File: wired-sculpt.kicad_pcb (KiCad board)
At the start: 2 copper layers, 40 x 50 mm, 26 parts, among them J1 10103594-0001LF, J3 AVR-ISP-6 - NOT FITTED, J4 3-84952-0, SW1 FSMSM, U1 AT90USB1286-AU, U2 USBLC6-2SC6, Y1 TSX-3225 16.0000MF18X-AC6

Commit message: WIP: checkpoint work on rev 3 of the schematic and layout
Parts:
- removed R4, R5, R6: ERJ-3GEYJ331V, Resistor_SMD:R_0603_1608Metric
- added C10: CL10A105KA8NNNC, Capacitor_SMD:C_0603_1608Metric, F.Cu at (157.2, 60.6)
- added C11: CL10A105KA8NNNC, Capacitor_SMD:C_0603_1608Metric, F.Cu at (156.2, 53.0)
- added C12: CL10A105KA8NNNC, Capacitor_SMD:C_0603_1608Metric, F.Cu at (157.7, 53.0)
- added C2: CL21B104KACNNNC, Capacitor_SMD:C_0805_2012Metric, F.Cu at (146.8, 67.0)
- added C3: CL21B103KBANNNC, Capacitor_SMD:C_0805_2012Metric, F.Cu at (146.8, 65.0)
- added Q1: BSS84AK,215, Package_TO_SOT_SMD:SOT-23, F.Cu at (137.4, 36.5)
- added Q2: 2N7002, Package_TO_SOT_SMD:SOT-23, F.Cu at (134.8, 40.1)
- added R10: ERJ-PA3J473V, Resistor_SMD:R_0603_1608Metric, F.Cu at (137.5, 34.0)
- added R11: ERJ-3GEYJ331V, Resistor_SMD:R_0603_1608Metric, F.Cu at (151.7, 41.7)
- added R12: ERJ-3EKF10R0V, Resistor_SMD:R_0603_1608Metric, F.Cu at (137.6, 40.1)
- added R13: ERJ-PA3J472V, Resistor_SMD:R_0603_1608Metric, F.Cu at (139.4, 40.1)
- added R7: ERJ-3EKF8873V, Resistor_SMD:R_0603_1608Metric, F.Cu at (145.2, 62.2)
- added SW2: Conn_01x02_Female, Connector_JST:JST_PH_S2B-PH-K_1x02_P2.00mm_Horizontal, F.Cu at (155.5, 67.0)
- added U3: LM2776, Package_TO_SOT_SMD:SOT-23-6, F.Cu at (156.7, 57.3)
- C1: value TAJA106K006RNJ -> CL21A475KAQNNNE; footprint Capacitor_Tantalum_SMD:CP_EIA-3216-10_Kemet-I -> Capacitor_SMD:C_0805_2012Metric
- C5, C6, C7: value CL05A104KA5NNNC -> CL10B104KB8NNNC; footprint Capacitor_SMD:C_0402_1005Metric -> Capacitor_SMD:C_0603_1608Metric
- R2: value ERJ-3EKF2200V -> ERJ-3GEYJ331V
- R8: value ERJ-3EKF1001V -> ERJ-3GEYJ103V
- moved D1 14.9 mm to (153.7, 35.4)
- moved U2 13.6 mm to (151.0, 71.9), turned to 90 degrees
- moved R2 12.3 mm to (151.7, 35.5), turned to 90 degrees
- moved J3 10.4 mm to (134.8, 76.4), turned to 90 degrees
- moved C1 8.35 mm to (146.8, 69.0), turned to 0 degrees
- moved R9 7.36 mm to (157.8, 47.0), turned to 90 degrees
- moved R1 6.04 mm to (151.8, 67.2)
- moved R8 6.00 mm to (133.8, 60.0)
- moved R3 5.95 mm to (150.1, 67.2)
- moved C4 2.35 mm to (154.4, 53.0), turned to 270 degrees
- moved C9 1.68 mm to (147.0, 38.0), turned to 135 degrees
- moved C8 1.65 mm to (142.2, 37.5), turned to 45 degrees
- moved Y1 0.92 mm to (144.6, 39.8), turned to 315 degrees
- moved C7 0.66 mm to (140.8, 62.2)
- moved C6 0.45 mm to (148.2, 41.5), turned to 0 degrees
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- renumbered C2 to C8, C3 to C9
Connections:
- C1 pad 1: VBUS -> GND
- C1 pad 2: GND -> VBUS
- J1 pad 2: Din- -> /Din-
- J1 pad 3: Din+ -> /Din+
- J3 pad 1: Net-(J3-Pad1) -> MISO
- J3 pad 3: Net-(J3-Pad3) -> SCK
- J3 pad 4: Net-(J3-Pad4) -> MOSI
- J4 pad 2: Net-(J4-Pad2) -> RED+
- J4 pad 3: Net-(J4-Pad3) -> GREEN-
- J4 pad MP: GND -> (no net)
- R1 pad 1: Net-(R1-Pad1) -> /D+
- R1 pad 2: Din+ -> /Dout+
- R3 pad 1: Net-(R3-Pad1) -> /D-
- R3 pad 2: Din- -> /Dout-
- R9 pad 1: Net-(R9-Pad1) -> RST
- R9 pad 2: RST -> Net-(R9-Pad2)
- SW1 pad 1: Net-(R9-Pad1) -> GND
- SW1 pad 2: GND -> Net-(R9-Pad2)
- U1 pad 10: Net-(U1-Pad10) -> PB0
- U1 pad 16: Net-(U1-Pad16) -> GREEN+
- U1 pad 17: Net-(U1-Pad17) -> RED+
- U1 pad 26: Net-(J4-Pad2) -> Net-(U1-Pad26)
- U1 pad 27: Net-(J4-Pad3) -> Net-(U1-Pad27)
- U1 pad 4: D- -> /D-
- U1 pad 5: D+ -> /D+
- U2 pad 1: D+ -> /Din-
- U2 pad 3: D- -> /Din+
- U2 pad 4: Net-(R3-Pad1) -> /Dout+
- U2 pad 6: Net-(R1-Pad1) -> /Dout-
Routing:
- net VBUS: track 75.5 -> 183.6 mm
- net Net-(R9-Pad2): track 0.00 -> 27.9 mm
- net RST: track 39.8 -> 12.6 mm
- net Net-(J3-Pad3): track 17.4 -> 0.00 mm
- net Net-(J4-Pad2): track 16.7 -> 0.00 mm
- net MOSI: track 22.1 -> 6.41 mm, vias 2 -> 0
- net Net-(J4-Pad3): track 15.6 -> 0.00 mm
- net /D+: track 0.00 -> 15.6 mm
- net /D-: track 0.00 -> 14.9 mm
- net MISO: track 23.4 -> 8.58 mm, vias 2 -> 0
- net Din-: track 13.4 -> 0.00 mm
- net Din+: track 13.1 -> 0.00 mm
- net PB0: track 0.00 -> 11.4 mm, vias 0 -> 2
- net SCK: track 21.1 -> 9.86 mm, vias 2 -> 0
- net Net-(J3-Pad1): track 9.49 -> 0.00 mm
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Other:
- board text added: "Wired Sculpt 0.3 Chad Austin 2020-03-06"
- board text removed: "Wired Sculpt 0.2 Chad Austin 2020-12-20"

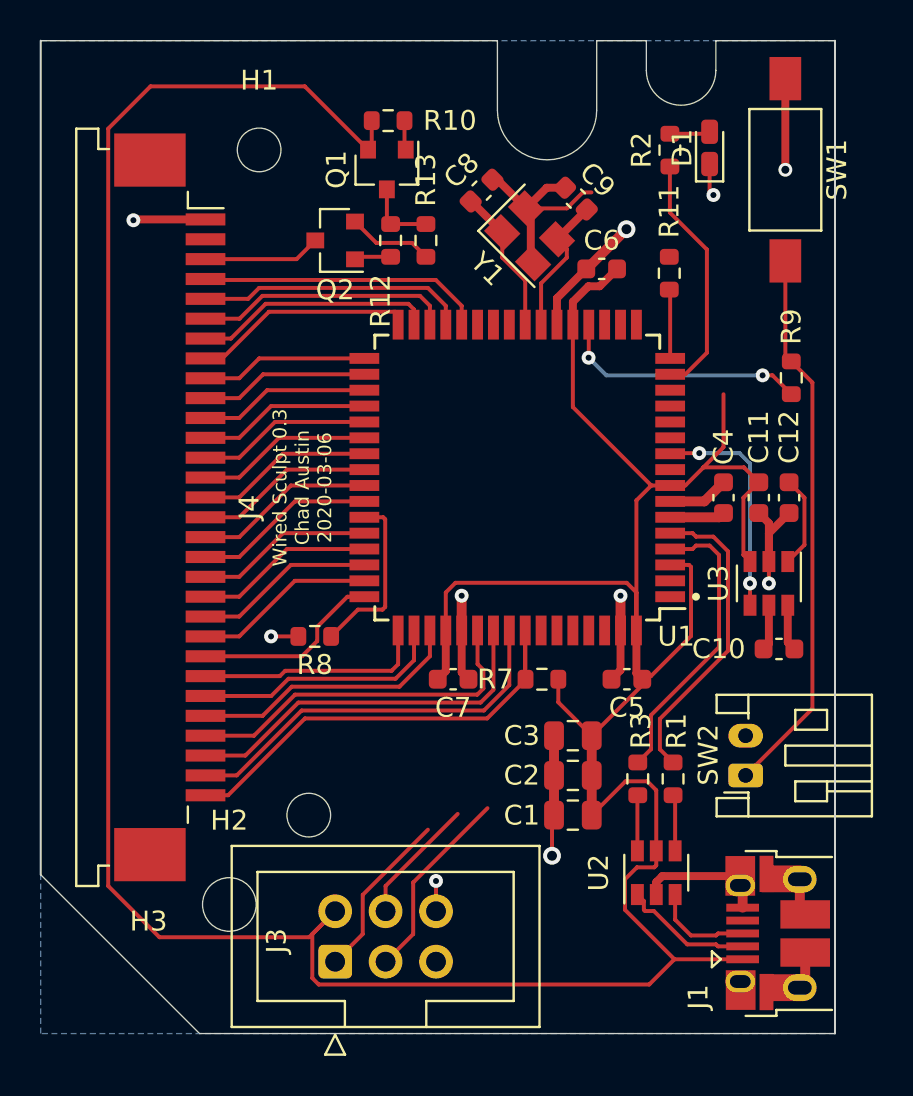
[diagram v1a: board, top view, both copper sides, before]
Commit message: renumber the references
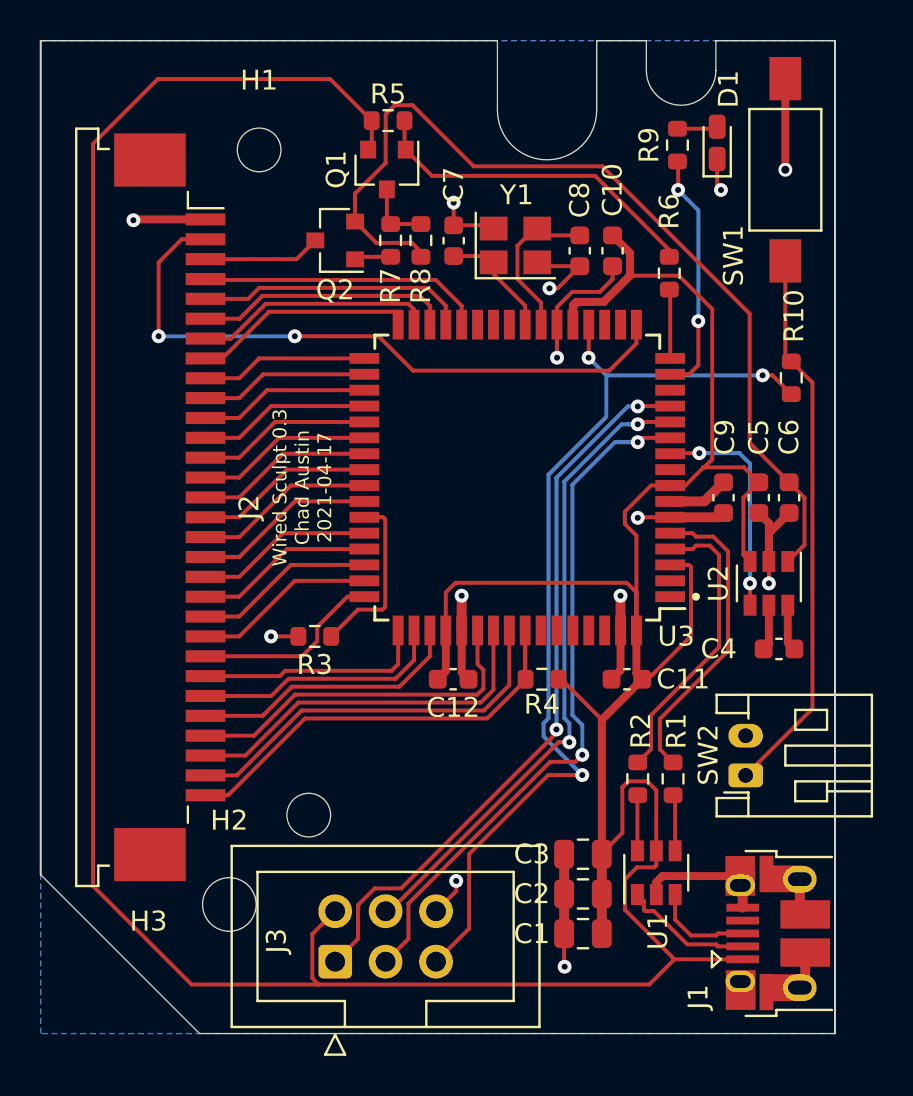
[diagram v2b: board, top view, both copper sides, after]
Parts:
- removed the R2 at (151.7, 35.5)
- added R9: ERJ-3GEYJ331V, Resistor_SMD:R_0603_1608Metric, F.Cu at (152.1, 35.3)
- moved C1 5.99 mm to (147.3, 75.0)
- moved C2 5.99 mm to (147.3, 73.0)
- moved C3 5.99 mm to (147.3, 71.0)
- moved C7 2.89 mm to (140.8, 40.1), turned to 90 degrees
- moved C8 2.63 mm to (147.1, 40.6), turned to 270 degrees
- moved C10 1.06 mm to (148.8, 40.6), turned to 90 degrees
- moved Y1 0.86 mm to (143.9, 40.3), turned to 0 degrees
- moved D1 0.46 mm to (154.1, 35.1)
- moved R8 0.25 mm to (139.1, 40.1)
- renumbered C6 to C10, C5 to C11, C7 to C12, C10 to C4, C11 to C5, C12 to C6, C8 to C7, C9 to C8, C4 to C9, J4 to J2, R9 to R10, R3 to R2, R8 to R3, R7 to R4, R10 to R5, R11 to R6, R12 to R7, R13 to R8, U2 to U1, U3 to U2, U1 to U3
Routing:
- net -5V: track 8.97 -> 47.2 mm
- net RST: track 12.6 -> 48.3 mm, vias 2 -> 3
- net RED+: track 0.00 -> 32.9 mm, vias 0 -> 2
- net MISO: track 8.58 -> 37.0 mm, vias 0 -> 2
- net MOSI: track 6.41 -> 33.1 mm, vias 0 -> 2
- net SCK: track 9.86 -> 35.0 mm, vias 0 -> 2
- net Net-(Q1-Pad1): track 1.49 -> 17.2 mm
- net VBUS: track 183.6 -> 198.2 mm
- net GND: track 64.6 -> 62.8 mm, vias 10 -> 13
- net Net-(C7-Pad1): track 7.36 -> 5.94 mm
- net Net-(C8-Pad1): track 7.16 -> 8.11 mm
- net LED: track 12.5 -> 12.4 mm, vias 0 -> 2
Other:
- board text added: "Wired Sculpt 0.3 Chad Austin 2021-04-17"
- board text removed: "Wired Sculpt 0.3 Chad Austin 2020-03-06"

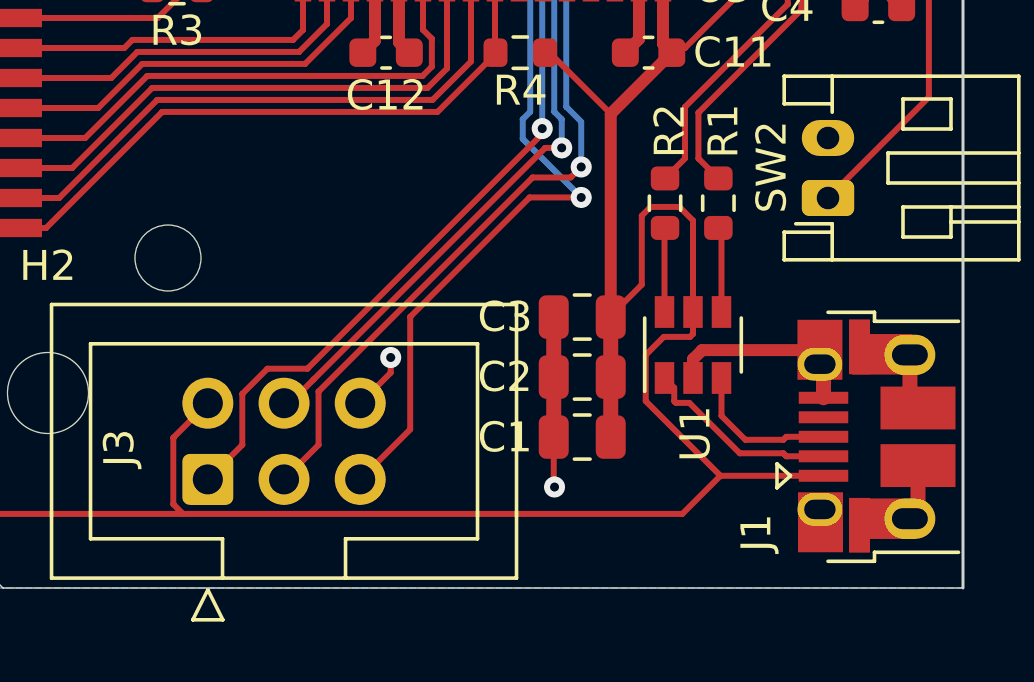
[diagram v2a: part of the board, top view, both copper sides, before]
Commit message: Move a trace and generate gerbers for Apr 18
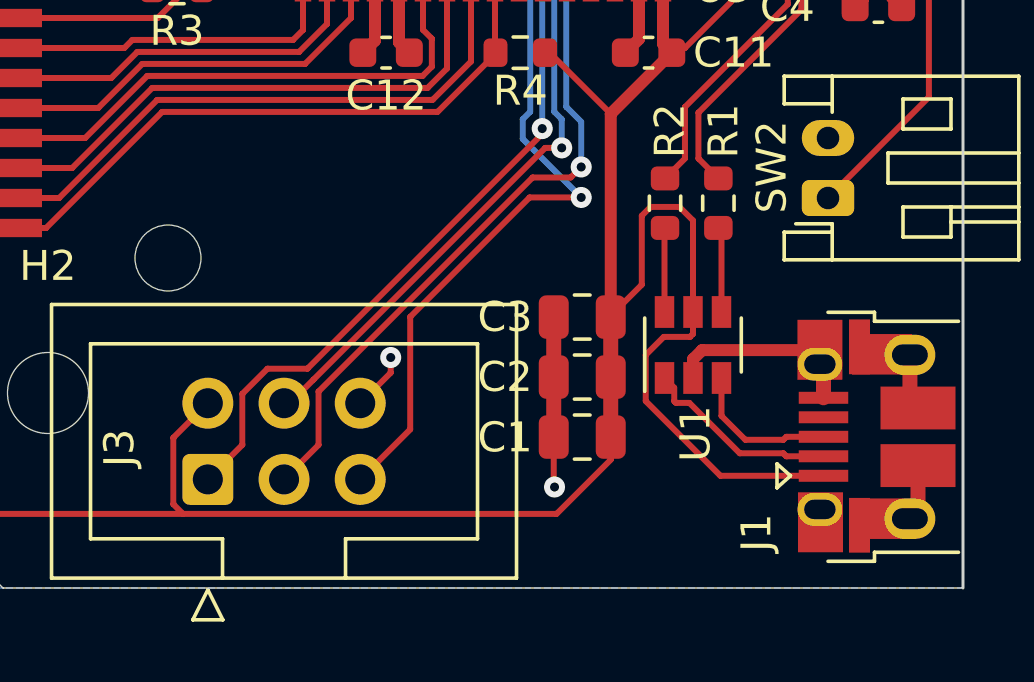
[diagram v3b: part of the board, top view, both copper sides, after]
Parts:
- J2: value 3-84952-0 -> FFC3B07-30-T
- Q2: value 2N7002 -> 2N7002BK
- R3: value ERJ-3GEYJ103V -> ERJ-PA3J472V
- SW2: value Conn_01x02_Female -> S2B-PH-K-S(LF)(SN)
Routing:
- net VBUS: track 198.2 -> 195.5 mm
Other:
- rule pad_to_mask_clearance: 0 -> 0.0508

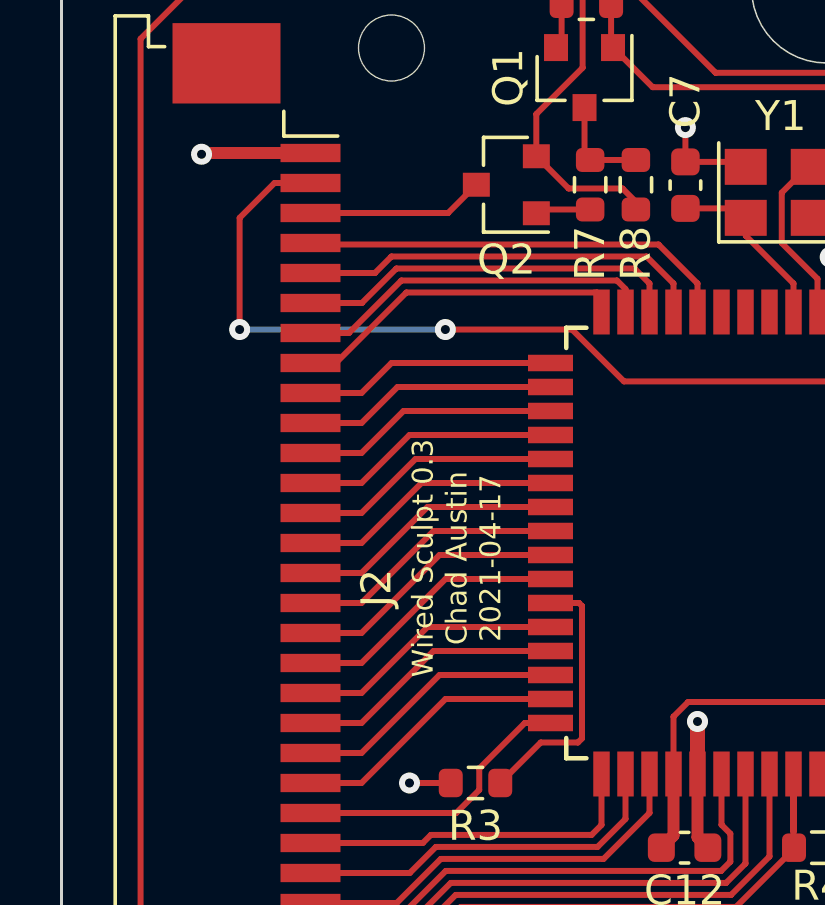
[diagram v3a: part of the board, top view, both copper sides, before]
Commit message: Fix Green- and Red+ pins which were backwards. :(
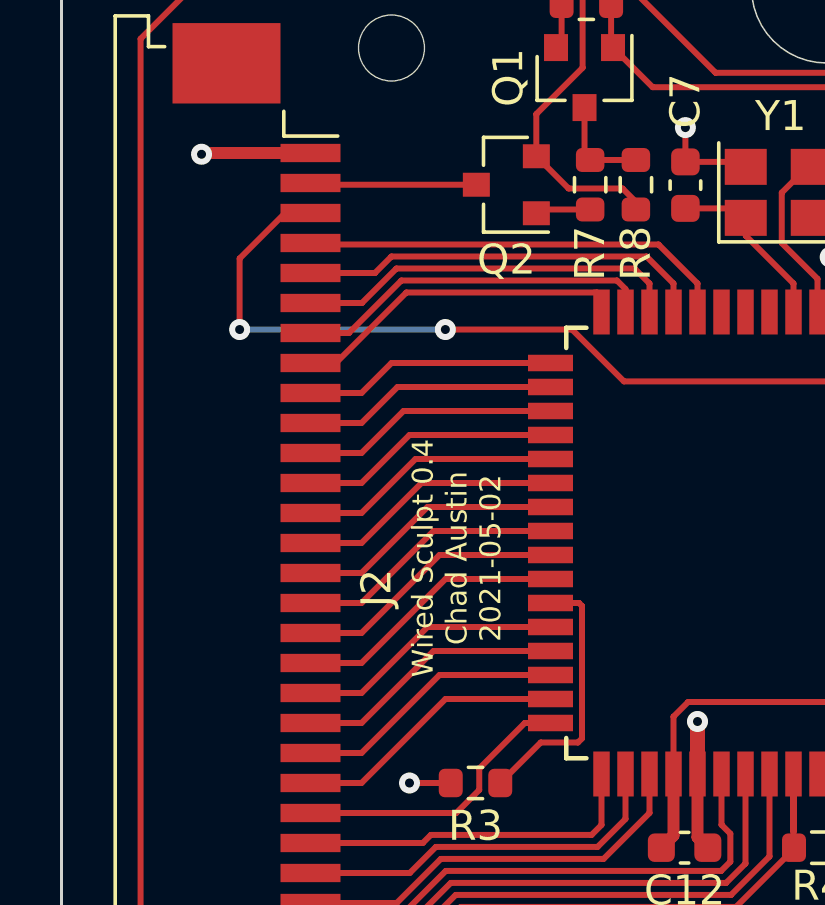
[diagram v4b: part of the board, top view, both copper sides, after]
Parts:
- C1: value CL21A475KAQNNNE -> CL21A475KOFNNNE
- C9: value C0603C105K4RACTU -> CL10A105KA8NNNC
- U2: value LM2776 -> LM2776DBVT
- Y1: value TSX-3225 16.0000MF18X-AC6 -> TSX-3225 16.0000MF18X-AC0
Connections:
- J2 pad 2: RED+ -> GREEN-
- J2 pad 3: GREEN- -> RED+
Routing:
- net RED+: track 32.9 -> 31.7 mm
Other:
- board text added: "Wired Sculpt 0.4 Chad Austin 2021-05-02"
- board text removed: "Wired Sculpt 0.3 Chad Austin 2021-04-17"

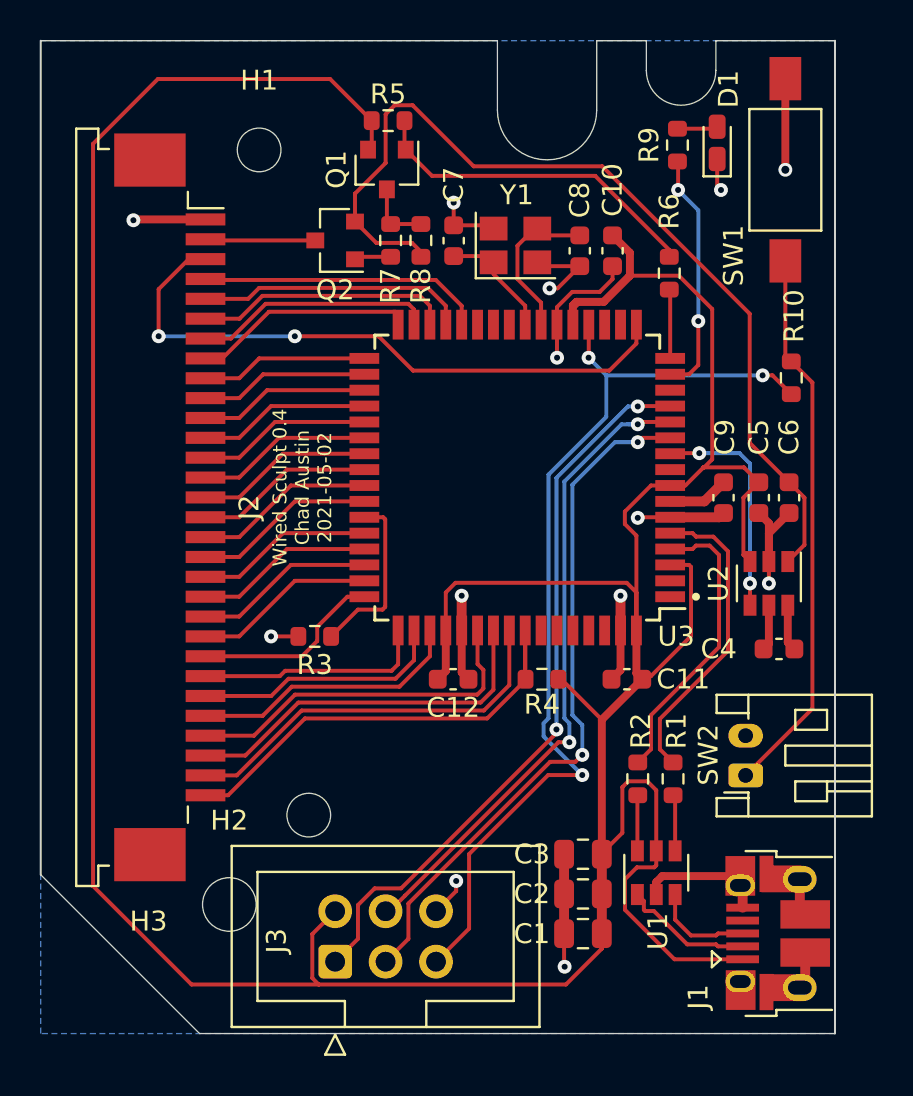
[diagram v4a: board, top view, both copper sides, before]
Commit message: add two resistors for the LEDs: this ribbon cable connector must have lower resistance
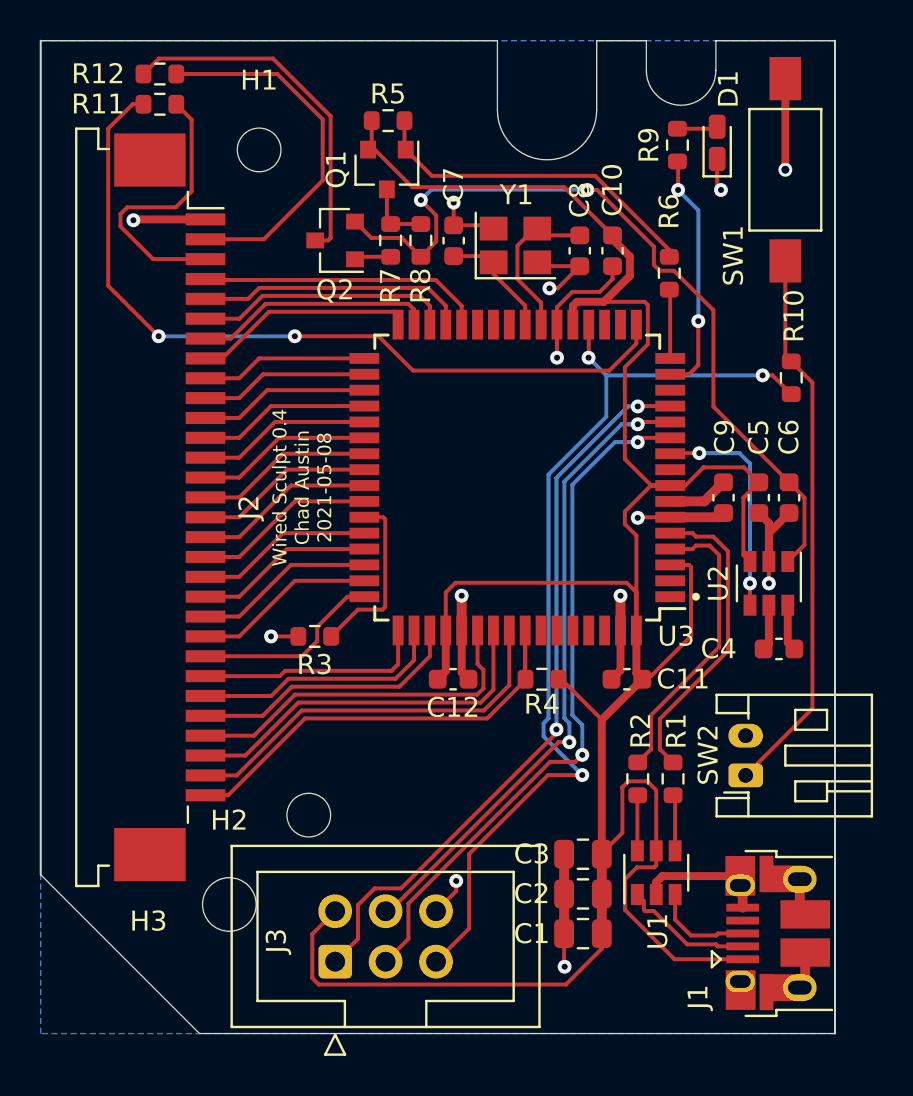
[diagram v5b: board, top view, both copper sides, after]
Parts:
- added R11: ERJ-PA3J560V, Resistor_SMD:R_0603_1608Metric, F.Cu at (126.0, 33.2)
- added R12: ERJ-PA3F22R0V, Resistor_SMD:R_0603_1608Metric, F.Cu at (126.0, 31.7)
- R7: value ERJ-3EKF10R0V -> ERJ-PA3F22R0V
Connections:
- J2 pad 2: GREEN- -> Net-(J2-Pad2)
- J2 pad 3: RED+ -> Net-(J2-Pad3)
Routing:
- net VBUS: track 195.5 -> 138.6 mm
- net Net-(J2-Pad2): track 0.00 -> 18.5 mm
- net Net-(J2-Pad3): track 0.00 -> 15.2 mm
- net GREEN-: track 5.55 -> 17.9 mm
- net RED+: track 31.7 -> 40.1 mm
- net -5V: track 47.2 -> 40.5 mm, vias 0 -> 2
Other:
- board text added: "Wired Sculpt 0.4 Chad Austin 2021-05-08"
- board text removed: "Wired Sculpt 0.4 Chad Austin 2021-05-02"
